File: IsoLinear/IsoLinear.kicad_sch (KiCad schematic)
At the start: 6 parts, among them U1 74HC164, U2 74HC164, U3 74HC164, U4 74LS251, U5 74LS251, U6 74LS75

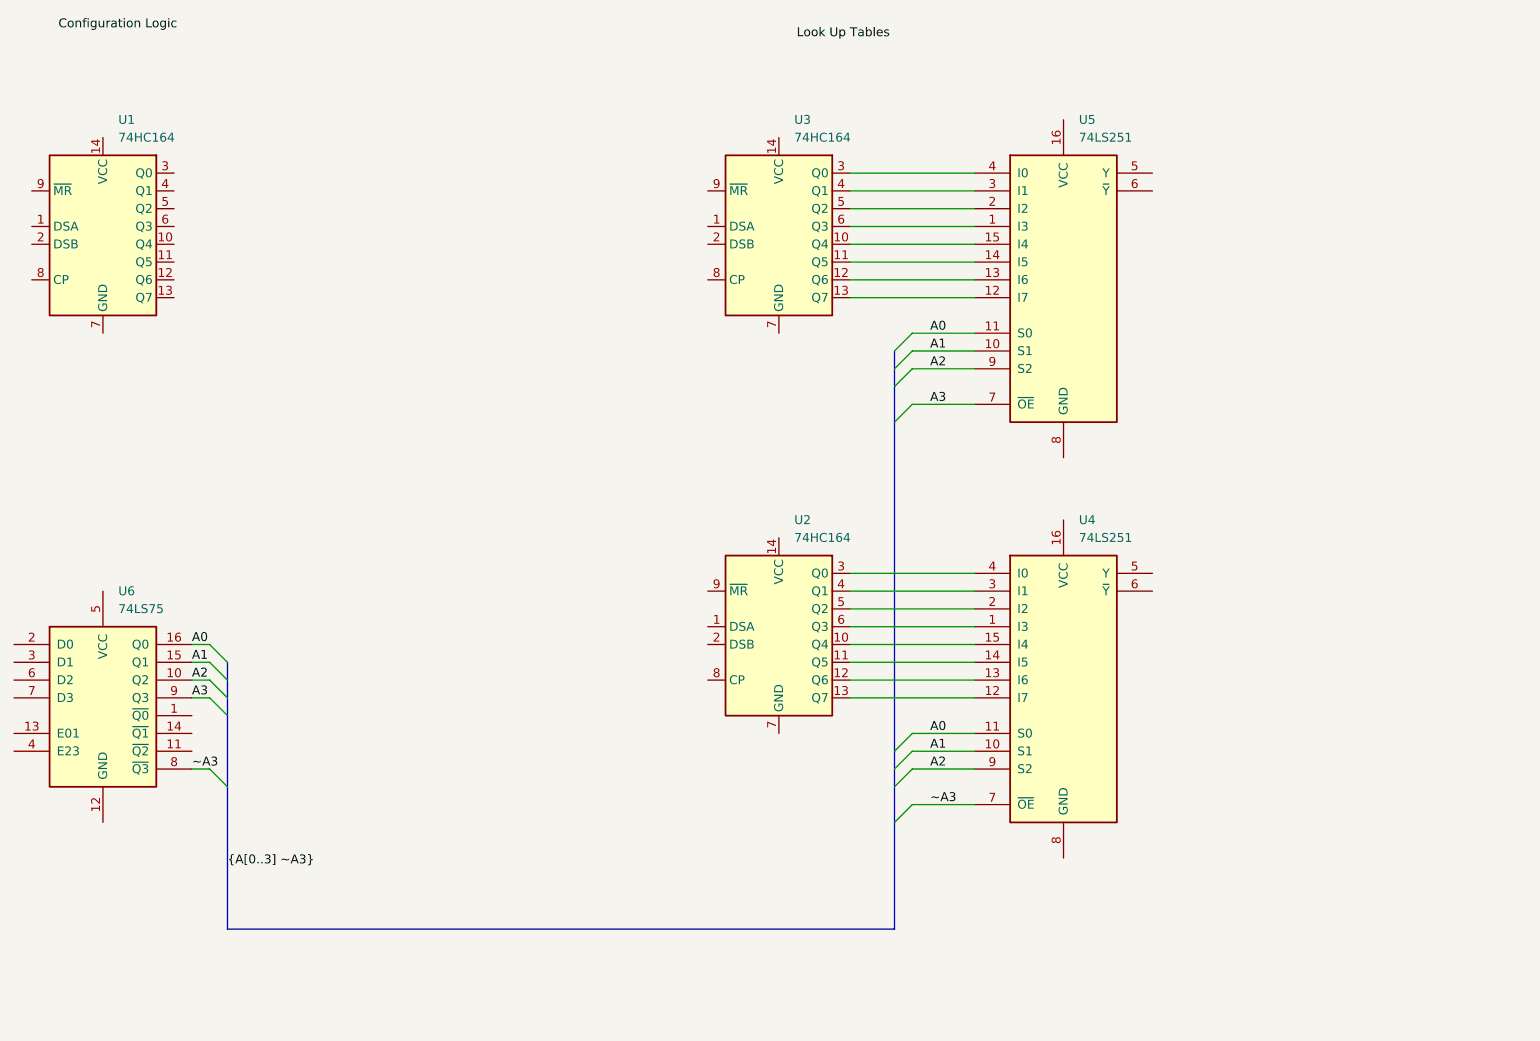
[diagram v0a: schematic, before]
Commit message: replace input latch with D flip flop
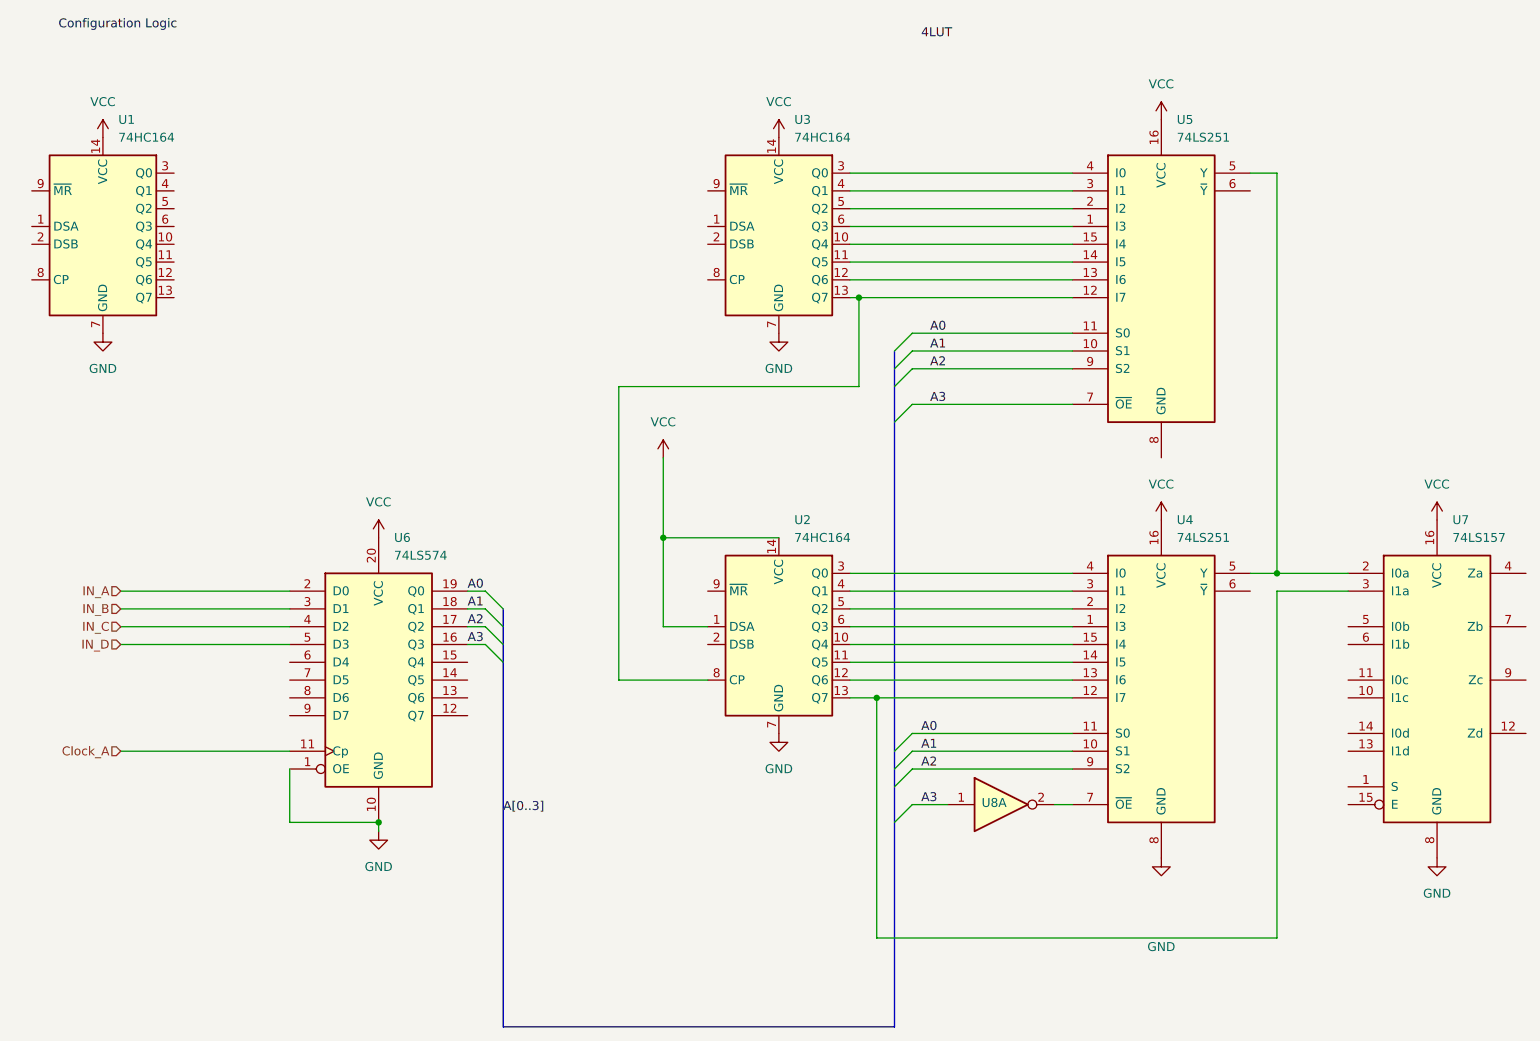
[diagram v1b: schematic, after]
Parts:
- removed U6: 74LS75, symbol 74xx:74LS75
- added U6: 74LS574, symbol 74xx:74LS574
- added U7: 74LS157, symbol 74xx:74LS157
- added U8: 74HC04, symbol 74xx:74HC04
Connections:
- net A0: now also U6.19 (Q0)
- net A1: now also U6.18 (Q1)
- net A2: now also U6.17 (Q2)
- net A3: now also U6.16 (Q3), U8.1
- net at U3.13 (Q7), U5.12 (I7): now also U2.8 (CP)
- net VCC: now reaches U3.14 (VCC)
- net VCC: now also U1.14 (VCC), U2.1 (DSA), U2.14 (VCC), U4.16 (VCC), U5.16 (VCC), U6.20 (VCC), U7.16 (VCC)
- net GND: now reaches U3.7 (GND)
- net GND: now also U1.7 (GND), U2.7 (GND), U4.8 (GND), U6.1 (OE), U6.10 (GND), U7.8 (GND)
- net at U5.5 (Y): now also U4.5 (Y), U7.2 (I0a)
- net at U2.13 (Q7), U4.12 (I7): now also U7.3 (I1a)
- net ~A3: no longer names the net of U4.7 (~{OE})
- net ~A3: now also U8.2
- new net Clock_A: U6.11 (Cp)
- new net IN_A: U6.2 (D0)
- new net IN_B: U6.3 (D1)
- new net IN_C: U6.4 (D2)
- new net IN_D: U6.5 (D3)
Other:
- moved on the sheet: U4, U5
